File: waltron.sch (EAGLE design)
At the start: 21 parts, among them IC1 4049N, U1 LM386

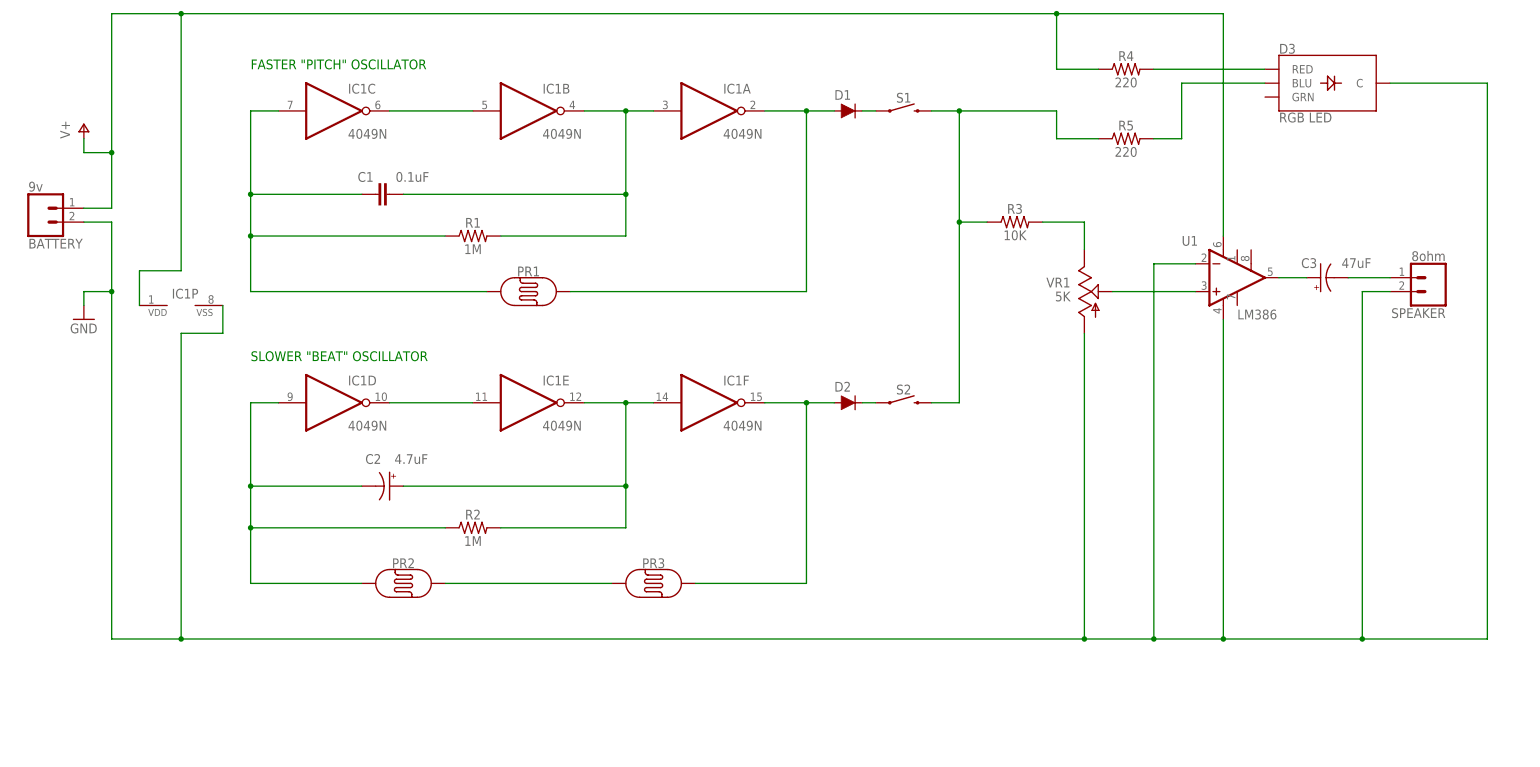
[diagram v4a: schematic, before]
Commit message: New layout, routed
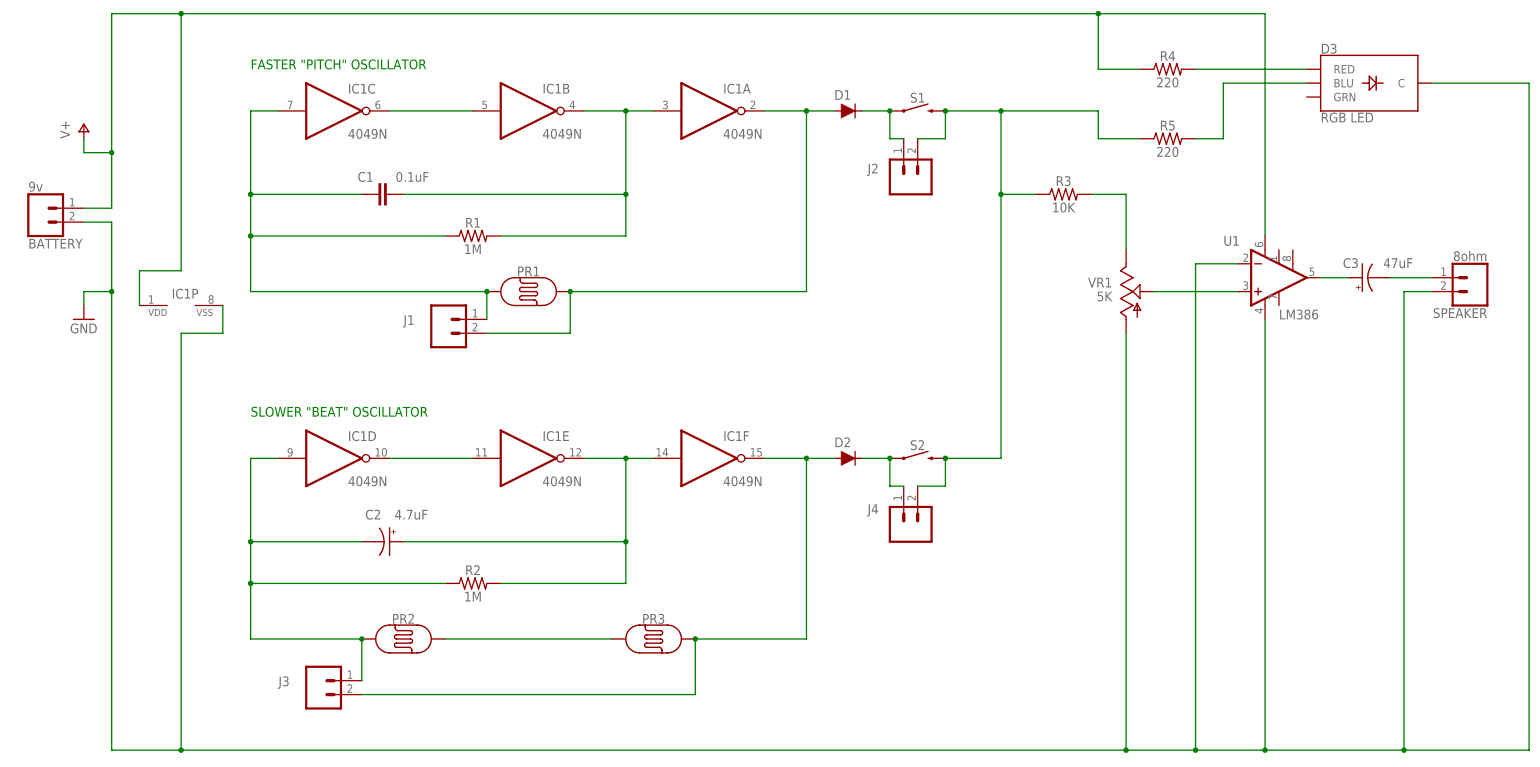
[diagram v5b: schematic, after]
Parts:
- added J1, J2, J3, J4: (no value), SparkFun-Connectors:CONN_02
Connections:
- net N$11: now also J4.1
- net N$12: now also J2.2, J4.2
- net N$3: now also J1.1
- net N$4: now also J1.2
- net N$5: now also J3.1
- net N$8: now also J3.2
- net N$9: now also J2.1
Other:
- moved on the sheet: C2, C3, D2, D3, IC1D, IC1E, IC1F, PR2, PR3, R2, R3, R4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

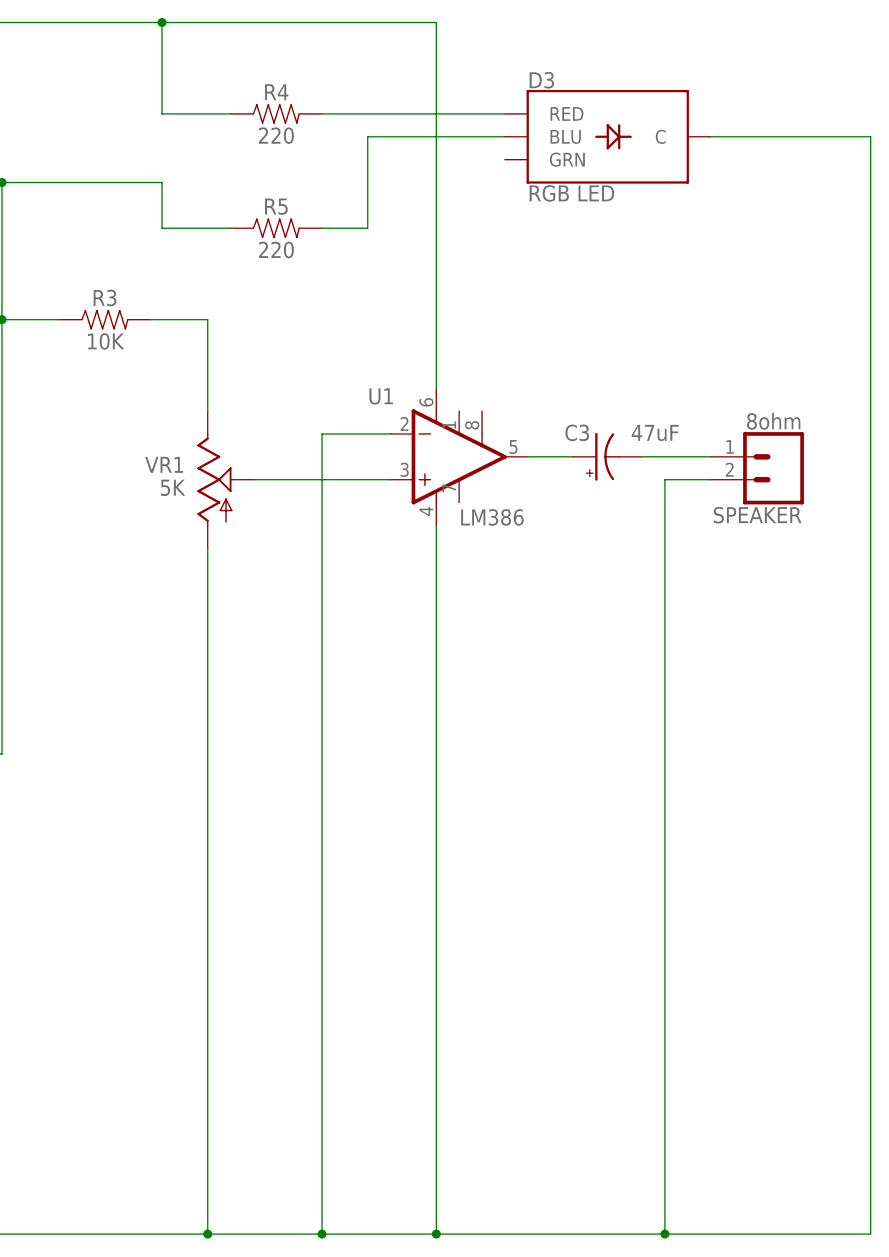
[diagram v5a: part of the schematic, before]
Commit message: Replaced D3 component w/ spaced leads
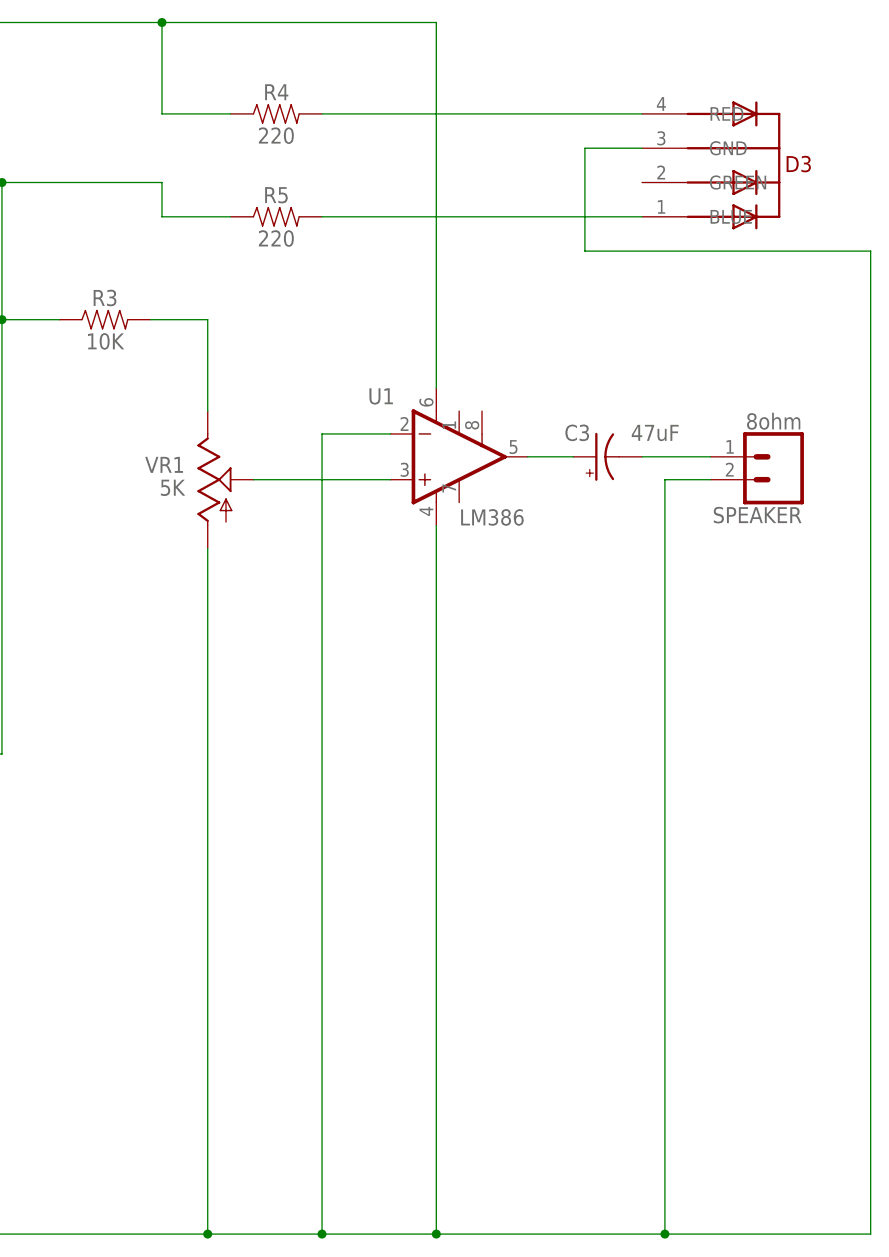
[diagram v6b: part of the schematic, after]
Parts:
- D3: value RGB LED -> 5MMRGBLED; device SparkFun-LED:LED-RGB-CCCLEAR -> adafruit:5MMRGBLED
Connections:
- net GND: now also D3.GND; no longer D3.C
- net N$17: now also D3.BLUE; no longer D3.BLU
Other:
- moved on the sheet: R5
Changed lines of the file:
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@@
 <setting verticaltext="up"/>
 </settings>
-<grid distance="0.1" unitdist="inch" unit="inch" style="lines" multiple="1" display="no" altdistance="0.01" altunitdist="inch" altunit="inch"/>
+<grid distance="0.000000123031" unitdist="inch" unit="inch" style="lines" multiple="1" display="no" altdistance="0.01" altunitdist="inch" altunit="inch"/>
 <layers>
 <layer number="1" name="Top" color="4" fill="1" visible="no" active="no"/>
@@
 <part name="BATTERY" library="SparkFun-Connectors" deviceset="CONN_02" device="" value="9v"/>
 <part name="SPEAKER" library="SparkFun-Connectors" deviceset="CONN_02" device="" value="8ohm"/>
-<part name="D3" library="SparkFun-LED" deviceset="LED-RGB-CC" device="CLEAR" value="RGB LED"/>
 <part name="R5" library="SparkFun-Resistors" deviceset="1KOHM" device="-HORIZ-1/4W-1%" value="220"/>
 <part name="R4" library="SparkFun-Resistors" deviceset="1KOHM" device="-HORIZ-1/4W-1%" value="220"/>
@@
 <part name="J3" library="SparkFun-Connectors" deviceset="CONN_02" device=""/>
 <part name="J4" library="SparkFun-Connectors" deviceset="CONN_02" device=""/>
+<part name="D3" library="adafruit" deviceset="5MMRGBLED" device=""/>
 </parts>
 <sheets>
@@
 <instance part="BATTERY" gate="G$1" x="-53.34" y="50.8" rot="MR180"/>
 <instance part="SPEAKER" gate="G$1" x="208.28" y="38.1" rot="R180"/>
-<instance part="D3" gate="G$1" x="187.96" y="73.66"/>
-<instance part="R5" gate="G$1" x="152.4" y="63.5"/>
+<instance part="R5" gate="G$1" x="152.4" y="64.77"/>
 <instance part="R4" gate="G$1" x="152.4" y="76.2"/>
 <instance part="R3" gate="G$1" x="133.35" y="53.34"/>
@@
 <attribute name="VALUE" x="99.314" y="-10.16" size="1.778" layer="96" font="vector" rot="MR90"/>
 <attribute name="NAME" x="99.568" y="-5.08" size="1.778" layer="95" font="vector" rot="MR0"/>
+</instance>
+<instance part="D3" gate="G$1" x="208.28" y="72.39" smashed="yes" rot="MR90">
+<attribute name="NAME" x="211.973553125" y="69.741753125" size="1.778" layer="94" rot="MR0"/>
 </instance>
 </instances>
@@
 <wire x1="121.92" y1="68.58" x2="139.7" y2="68.58" width="0.1524" layer="91"/>
 <junction x="121.92" y="68.58"/>
-<wire x1="139.7" y1="68.58" x2="139.7" y2="63.5" width="0.1524" layer="91"/>
+<wire x1="139.7" y1="68.58" x2="139.7" y2="64.77" width="0.1524" layer="91"/>
 <pinref part="R5" gate="G$1" pin="1"/>
-<wire x1="139.7" y1="63.5" x2="147.32" y2="63.5" width="0.1524" layer="91"/>
+<wire x1="139.7" y1="64.77" x2="147.32" y2="64.77" width="0.1524" layer="91"/>
 <pinref part="J2" gate="G$1" pin="2"/>
 <wire x1="106.68" y1="63.5" x2="111.76" y2="63.5" width="0.1524" layer="91"/>
@@
 <segment>
 <pinref part="R5" gate="G$1" pin="2"/>
-<wire x1="157.48" y1="63.5" x2="162.56" y2="63.5" width="0.1524" layer="91"/>
-<wire x1="162.56" y1="63.5" x2="162.56" y2="73.66" width="0.1524" layer="91"/>
-<pinref part="D3" gate="G$1" pin="BLU"/>
-<wire x1="162.56" y1="73.66" x2="177.8" y2="73.66" width="0.1524" layer="91"/>
-</segment>
-</net>
-<net name="N$18" class="0">
-<segment>
-<pinref part="R4" gate="G$1" pin="2"/>
-<pinref part="D3" gate="G$1" pin="RED"/>
-<wire x1="157.48" y1="76.2" x2="177.8" y2="76.2" width="0.1524" layer="91"/>
+<wire x1="157.48" y1="64.77" x2="193.04" y2="64.77" width="0.1524" layer="91"/>
+<pinref part="D3" gate="G$1" pin="BLUE"/>
 </segment>
 </net>
@@
 <wire x1="195.58" y1="-48.26" x2="218.44" y2="-48.26" width="0.1524" layer="91"/>
 <junction x="195.58" y="-48.26"/>
-<wire x1="218.44" y1="-48.26" x2="218.44" y2="73.66" width="0.1524" layer="91"/>
-<pinref part="D3" gate="G$1" pin="C"/>
-<wire x1="218.44" y1="73.66" x2="200.66" y2="73.66" width="0.1524" layer="91"/>
+<wire x1="218.44" y1="-48.26" x2="218.44" y2="60.96" width="0.1524" layer="91"/>
 <pinref part="BATTERY" gate="G$1" pin="2"/>
 <wire x1="-45.72" y1="48.26" x2="-40.64" y2="48.26" width="0.1524" layer="91"/>
@@
 <junction x="144.78" y="-48.26"/>
 <wire x1="144.78" y1="27.94" x2="144.78" y2="-48.26" width="0.1524" layer="91"/>
+<pinref part="D3" gate="G$1" pin="GND"/>
+<wire x1="193.04" y1="72.39" x2="186.69" y2="72.39" width="0.1524" layer="91"/>
+<wire x1="186.69" y1="72.39" x2="186.69" y2="60.96" width="0.1524" layer="91"/>
+<wire x1="186.69" y1="60.96" x2="218.44" y2="60.96" width="0.1524" layer="91"/>
 </segment>
 </net>
@@
 </segment>
 </net>
+<net name="N$18" class="0">
+<segment>
+<pinref part="R4" gate="G$1" pin="2"/>
+<pinref part="D3" gate="G$1" pin="RED"/>
+<wire x1="157.48" y1="76.2" x2="193.04" y2="76.2" width="0.1524" layer="91"/>
+</segment>
+</net>
